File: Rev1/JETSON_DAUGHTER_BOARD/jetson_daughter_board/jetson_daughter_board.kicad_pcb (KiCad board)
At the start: 2 copper layers, 11.9 x 10.3 mm, 2 parts, among them J1 F3311A7H121014E200, J2 TFML-105-01-L-D-RA

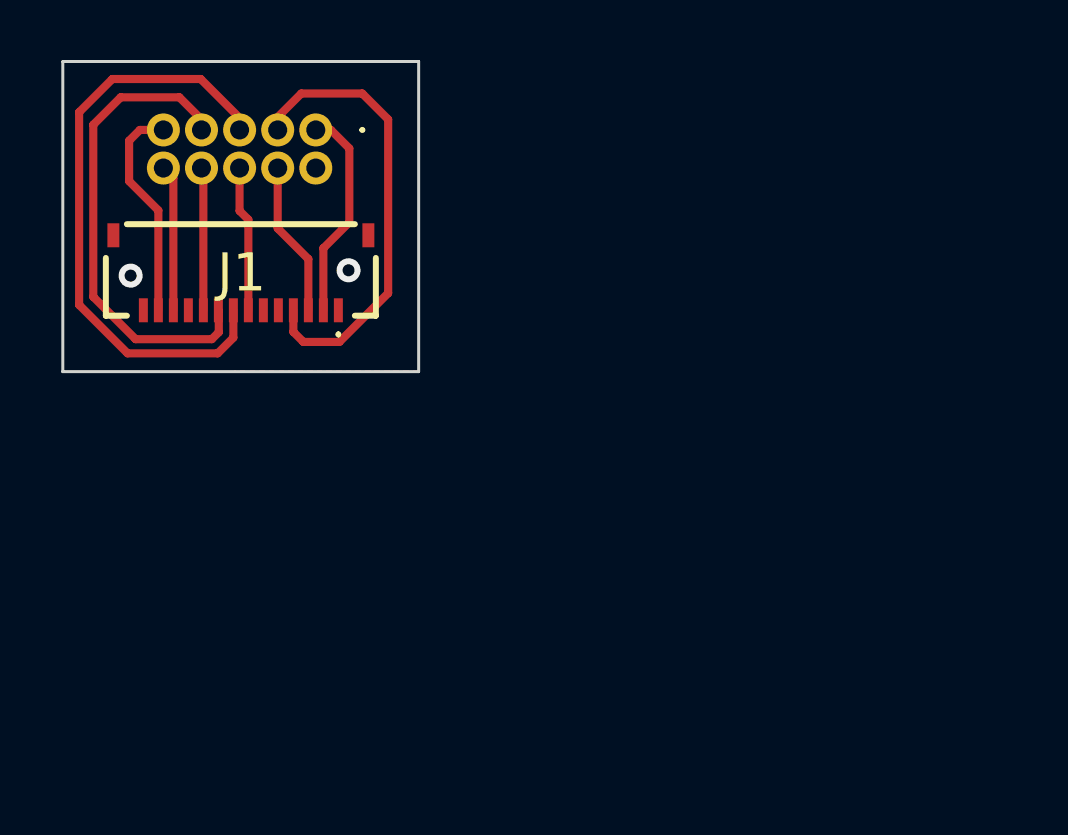
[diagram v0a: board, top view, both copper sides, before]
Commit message: Updated USB HUB
Based on Mechanical Feedback
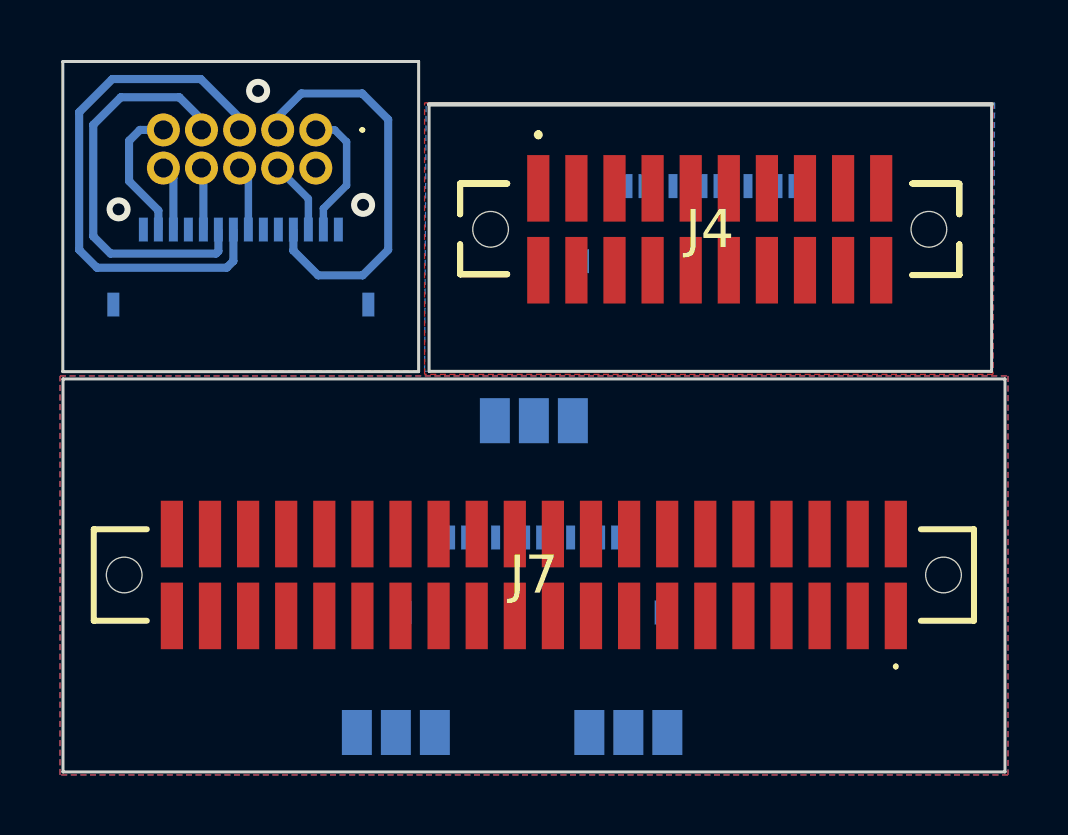
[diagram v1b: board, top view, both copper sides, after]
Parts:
- added J3: F3311A7H121014E200, SamacSys_Parts:F3311A7H121014E200, B.Cu at (122.6, 52.9)
- added J4: SFM-110-02-L-D-LC-K, SamacSys_Parts:SFM11002LDLCK, F.Cu at (122.6, 53.0)
- added J5: PYCUBED, SamacSys_Parts:F3311A7H121014E200, B.Cu at (116.7, 64.6)
- added J7: SFM-120-02-L-D-LC-K, SamacSys_Parts:SFM12002LDLCK, F.Cu at (116.7, 64.5)
- added JP1: SolderJumper_3_Open, Jumper:SolderJumper-3_P1.3mm_Open_Pad1.0x1.5mm, B.Cu at (119.8, 69.8)
- added JP2: SolderJumper_3_Open, Jumper:SolderJumper-3_P1.3mm_Open_Pad1.0x1.5mm, B.Cu at (112.1, 69.8)
- added JP3: SolderJumper_3_Open, Jumper:SolderJumper-3_P1.3mm_Open_Pad1.0x1.5mm, B.Cu at (116.7, 59.4)
- J1: value F3311A7H121014E200 -> PYCUBED; moved to B.Cu
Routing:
- net DAC0: track 7.13 -> 4.44 mm
- net RX: track 5.16 -> 2.47 mm
- net SDA2_JETSON: track 4.88 -> 2.19 mm
- net SCL2_JETSON: track 7.35 -> 4.66 mm
- net JETSON_RX: track 4.86 -> 2.17 mm
- net AIN5: track 4.79 -> 2.10 mm
- net JETSON_TX: track 16.0 -> 13.5 mm
- net JETSON_XCK: track 20.1 -> 17.9 mm
- net TX: track 15.3 -> 13.7 mm
- net GND: vias 2 -> 3
- added copper zone on B.Cu, net GND1
- added copper zone on F.Cu, net GND1
- added copper zone on B.Cu, net GND2
- added copper zone on F.Cu, net GND2
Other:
- board size 11.9 x 10.3 mm -> 31.4 x 23.7 mm
- rule pad_to_mask_clearance: 0 -> 0.0508

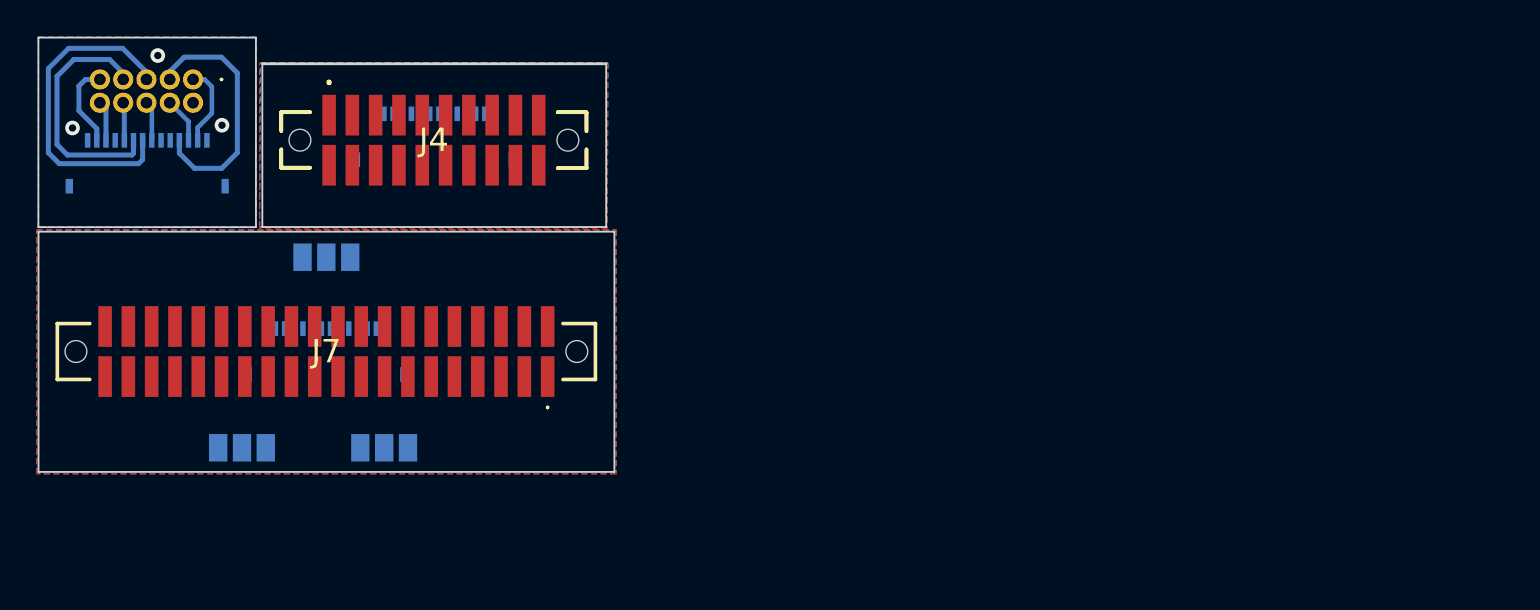
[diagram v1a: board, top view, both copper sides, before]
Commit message: USB_HUB Thickness Changed
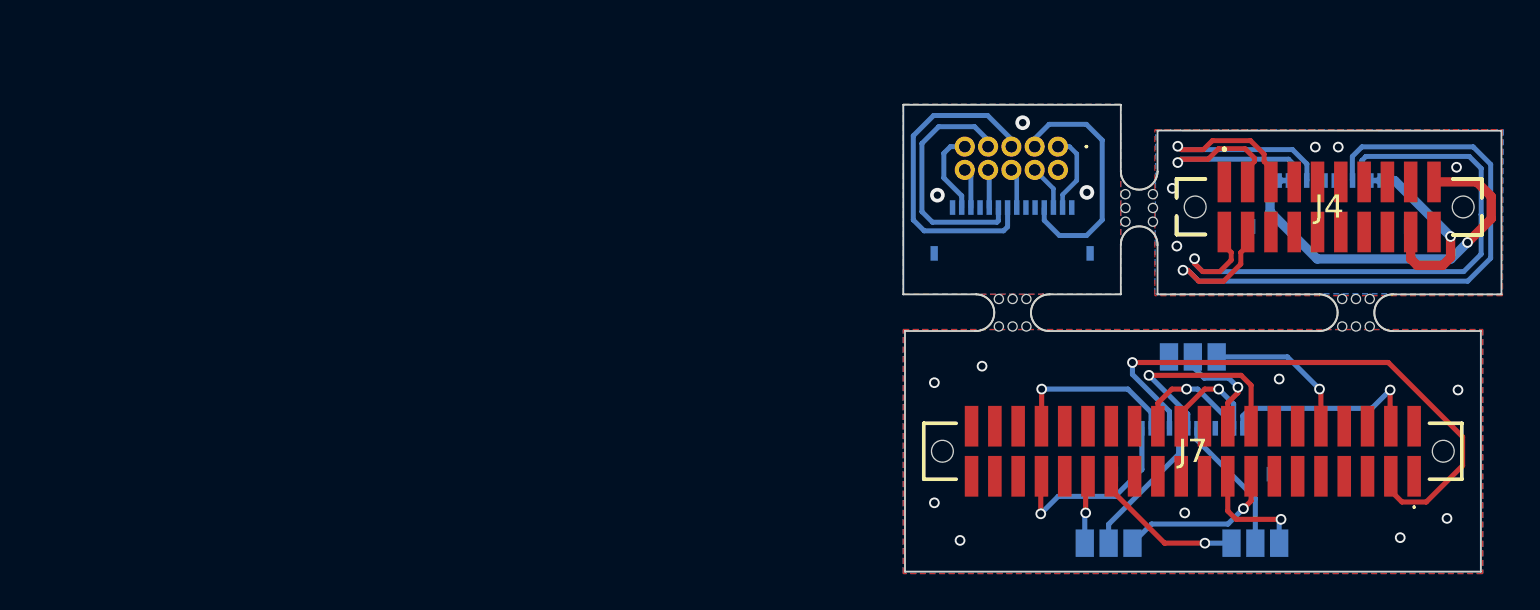
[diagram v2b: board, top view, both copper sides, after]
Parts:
- added mouse-bite-2mm-slot: VAL**, Panelization:mouse-bite-2mm-slot, F.Cu at (172.8, 62.4)
- added mouse-bite-2mm-slot: VAL**, Panelization:mouse-bite-2mm-slot, F.Cu at (161.0, 56.7)
- added mouse-bite-2mm-slot: VAL**, Panelization:mouse-bite-2mm-slot, F.Cu at (154.1, 62.4)
- moved JP2 55.5 mm to (167.3, 75.0)
- moved J3 48.9 mm to (171.4, 56.6)
- moved J4 48.9 mm to (171.4, 56.7)
- moved J5 47.6 mm to (163.9, 70.1)
- moved J7 47.6 mm to (163.9, 70.0)
- moved JP3 47.6 mm to (163.9, 64.8)
- moved J1 47.3 mm to (154.1, 58.0)
- moved J2 47.3 mm to (156.6, 53.4)
- moved JP1 39.8 mm to (159.3, 75.0)
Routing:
- net /P2-: track 0.00 -> 37.8 mm, vias 0 -> 1
- net /P2+: track 0.00 -> 33.5 mm, vias 0 -> 1
- net AIN5_1: track 0.00 -> 31.5 mm, vias 0 -> 1
- net Net-(J3-Pad12): track 0.00 -> 21.4 mm, vias 0 -> 1
- net /P1-: track 0.00 -> 15.3 mm, vias 0 -> 1
- net /P1+: track 0.00 -> 13.6 mm, vias 0 -> 1
- net JETSON_XCK_1: track 0.00 -> 11.8 mm, vias 0 -> 1
- net DAC0_1: track 0.00 -> 11.3 mm, vias 0 -> 1
- net SCL2_JETSON_1: track 0.00 -> 10.8 mm, vias 0 -> 1
- net Net-(J3-Pad1): track 0.00 -> 10.7 mm, vias 0 -> 1
- net SDA2_JETSON_1: track 0.00 -> 9.39 mm, vias 0 -> 1
- net Net-(JP1-B): track 0.00 -> 8.77 mm, vias 0 -> 1
- net Net-(JP2-A): track 0.00 -> 8.50 mm, vias 0 -> 1
- net Net-(JP3-A): track 0.00 -> 8.39 mm, vias 0 -> 1
- net JETSON_TX_1: track 0.00 -> 7.84 mm
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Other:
- board size 31.4 x 23.7 mm -> 32.6 x 25.5 mm
